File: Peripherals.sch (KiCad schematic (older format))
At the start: 62 parts, among them J10 Conn_01x01, J11 Conn_01x01, J12 Conn_01x01, J13 Conn_01x04, J14 RCAJack, J5 Conn_01x10, J6 Conn_01x10, J7 Conn_01x10, J8 Conn_01x08, J9 Conn_01x01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

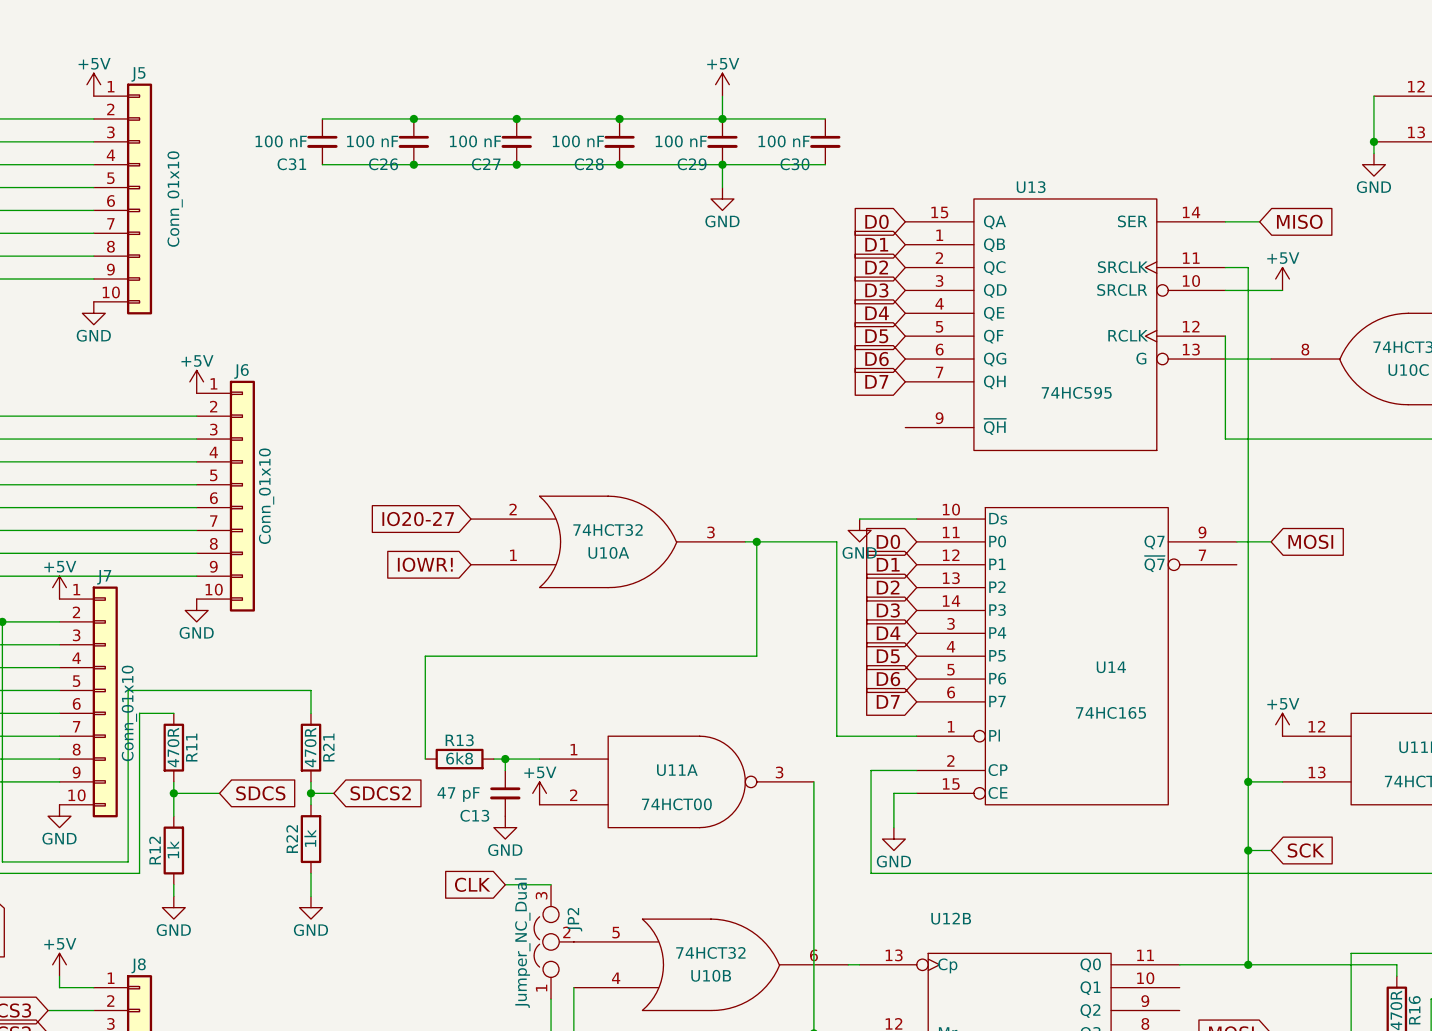
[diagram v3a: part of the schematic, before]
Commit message: Added SD card driver
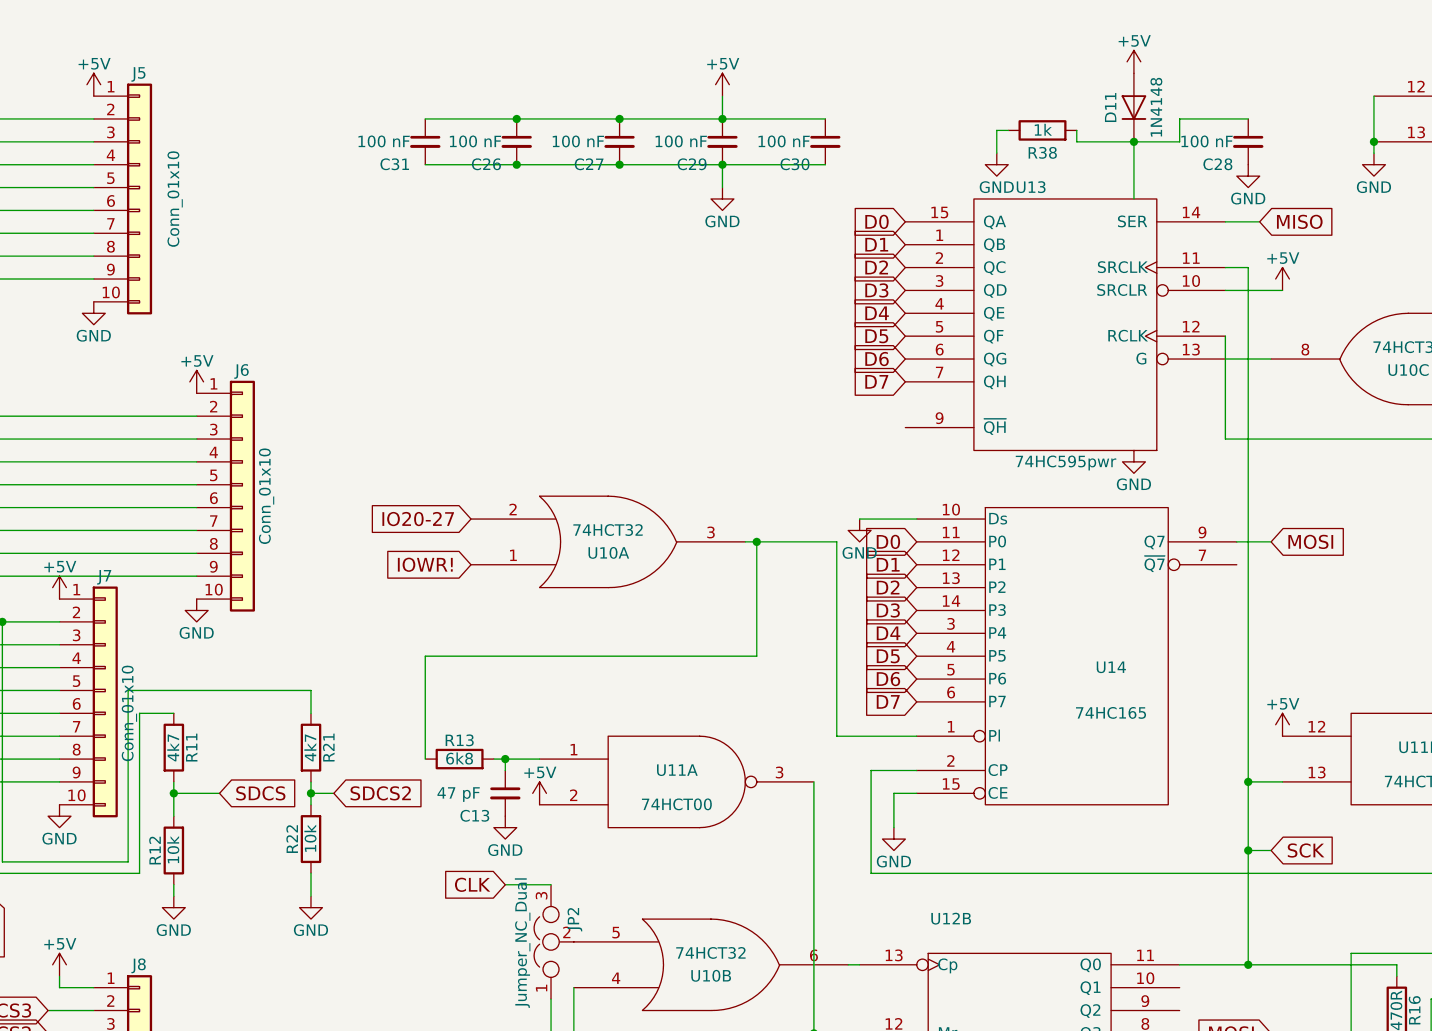
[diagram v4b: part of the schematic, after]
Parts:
- removed U13: 74HC595, Housings_DIP:DIP-16_W7.62mm_Socket, symbol 74HC595
- added D11: 1N4148, Diodes_THT:D_DO-35_SOD27_P7.62mm_Horizontal, symbol D
- added R38: 1k, Resistors_THT:R_Axial_DIN0207_L6.3mm_D2.5mm_P7.62mm_Horizontal, symbol R
- added U13: 74HC595pwr, symbol 74HC595pwr
- R11, R21: value 470R -> 4k7
- R12, R22: value 1k -> 10k
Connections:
- net +5V: now also D11.2 (A), U13.10 (SRCLR); no longer C28.1
- net D0: now also U13.15 (QA)
- net D1: now also U13.1 (QB)
- net D2: now also U13.2 (QC)
- net D3: now also U13.3 (QD)
- net D4: now also U13.4 (QE)
- net D5: now also U13.5 (QF)
- net D6: now also U13.6 (QG)
- net D7: now also U13.7 (QH)
- net GND: now also R38.1, U13.8 (GND)
- net MISO: now also U13.14 (SER)
- net SCK: now also U13.11 (SRCLK)
- net at U11.11, U14.2 (CP): now also U13.12 (RCLK)
- net at U10.8: now also U13.13 (G)
- new net: C28.1, D11.1 (K), R38.2, U13.16 (VCC)
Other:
- moved on the sheet: C26, C27, C28, C31
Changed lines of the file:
@@
 D7
 $Comp
-L +5V #PWR89
+L +5V #PWR92
 U 1 1 607EE7EE
 P 8950 1650
-F 0 "#PWR89" H 8950 1500 50  0001 C CNN
+F 0 "#PWR92" H 8950 1500 50  0001 C CNN
 F 1 "+5V" H 8950 1790 50  0000 C CNN
 F 2 "" H 8950 1650 50  0001 C CNN
@@
 	1    0    0    -1
 $EndComp
-$Comp
-L 74HC595 U13
-U 1 1 607EE4CE
-P 8000 1800
-F 0 "U13" H 8150 2400 50  0000 C CNN
-F 1 "74HC595" H 7950 1500 50  0000 C CNN
-F 2 "Housings_DIP:DIP-16_W7.62mm_Socket" H 8000 1800 50  0001 C CNN
-F 3 "" H 8000 1800 50  0001 C CNN
-	1    8000 1800
-	-1   0    0    -1
-$EndComp
 Text GLabel 8900 4900 0    60   Input ~ 0
 MOSI
@@
 $EndComp
 $Comp
-L GND #PWR91
+L GND #PWR94
 U 1 1 607928DE
 P 9050 5600
-F 0 "#PWR91" H 9050 5350 50  0001 C CNN
+F 0 "#PWR94" H 9050 5350 50  0001 C CNN
 F 1 "GND" H 9050 5450 50  0000 C CNN
 F 2 "" H 9050 5600 50  0001 C CNN
@@
 MISO
 $Comp
-L GND #PWR95
+L GND #PWR98
 U 1 1 60792D6A
 P 10050 6150
-F 0 "#PWR95" H 10050 5900 50  0001 C CNN
+F 0 "#PWR98" H 10050 5900 50  0001 C CNN
 F 1 "GND" H 10050 6000 50  0000 C CNN
 F 2 "" H 10050 6150 50  0001 C CNN
@@
 $EndComp
 $Comp
-L +5V #PWR97
+L +5V #PWR100
 U 1 1 60792FF2
 P 10350 2800
-F 0 "#PWR97" H 10350 2650 50  0001 C CNN
+F 0 "#PWR100" H 10350 2650 50  0001 C CNN
 F 1 "+5V" H 10350 2940 50  0000 C CNN
 F 2 "" H 10350 2800 50  0001 C CNN
@@
 $EndComp
 $Comp
-L GND #PWR94
+L GND #PWR97
 U 1 1 60793535
 P 9450 5350
-F 0 "#PWR94" H 9450 5100 50  0001 C CNN
+F 0 "#PWR97" H 9450 5100 50  0001 C CNN
 F 1 "GND" H 9450 5200 50  0000 C CNN
 F 2 "" H 9450 5350 50  0001 C CNN
@@
 $EndComp
 $Comp
-L GND #PWR98
+L GND #PWR101
 U 1 1 60794114
 P 10350 3850
-F 0 "#PWR98" H 10350 3600 50  0001 C CNN
+F 0 "#PWR101" H 10350 3600 50  0001 C CNN
 F 1 "GND" H 10350 3700 50  0000 C CNN
 F 2 "" H 10350 3850 50  0001 C CNN
@@
 $EndComp
 $Comp
-L GND #PWR99
+L GND #PWR102
 U 1 1 607945EF
 P 10900 3900
-F 0 "#PWR99" H 10900 3650 50  0001 C CNN
+F 0 "#PWR102" H 10900 3650 50  0001 C CNN
 F 1 "GND" H 10900 3750 50  0000 C CNN
 F 2 "" H 10900 3900 50  0001 C CNN
@@
 P 4100 3650
 F 0 "R11" V 4180 3650 50  0000 C CNN
-F 1 "470R" V 4100 3650 50  0000 C CNN
+F 1 "4k7" V 4100 3650 50  0000 C CNN
 F 2 "Resistors_THT:R_Axial_DIN0207_L6.3mm_D2.5mm_P7.62mm_Horizontal" V 4030 3650 50  0001 C CNN
 F 3 "" H 4100 3650 50  0001 C CNN
@@
 P 4100 4100
 F 0 "R12" V 4180 4100 50  0000 C CNN
-F 1 "1k" V 4100 4100 50  0000 C CNN
+F 1 "10k" V 4100 4100 50  0000 C CNN
 F 2 "Resistors_THT:R_Axial_DIN0207_L6.3mm_D2.5mm_P7.62mm_Horizontal" V 4030 4100 50  0001 C CNN
 F 3 "" H 4100 4100 50  0001 C CNN
@@
 $EndComp
 $Comp
-L +5V #PWR90
+L +5V #PWR93
 U 1 1 607AC0B6
 P 8950 3600
-F 0 "#PWR90" H 8950 3450 50  0001 C CNN
+F 0 "#PWR93" H 8950 3450 50  0001 C CNN
 F 1 "+5V" H 8950 3740 50  0000 C CNN
 F 2 "" H 8950 3600 50  0001 C CNN
@@
 P 4700 3650
 F 0 "R21" V 4780 3650 50  0000 C CNN
-F 1 "470R" V 4700 3650 50  0000 C CNN
+F 1 "4k7" V 4700 3650 50  0000 C CNN
 F 2 "Resistors_THT:R_Axial_DIN0207_L6.3mm_D2.5mm_P7.62mm_Horizontal" V 4630 3650 50  0001 C CNN
 F 3 "" H 4700 3650 50  0001 C CNN
@@
 P 4700 4050
 F 0 "R22" V 4780 4050 50  0000 C CNN
-F 1 "1k" V 4700 4050 50  0000 C CNN
+F 1 "10k" V 4700 4050 50  0000 C CNN
 F 2 "Resistors_THT:R_Axial_DIN0207_L6.3mm_D2.5mm_P7.62mm_Horizontal" V 4630 4050 50  0001 C CNN
 F 3 "" H 4700 4050 50  0001 C CNN
@@
 SDCS2
 $Comp
-L GND #PWR96
+L GND #PWR99
 U 1 1 607C336C
 P 10100 5150
-F 0 "#PWR96" H 10100 4900 50  0001 C CNN
+F 0 "#PWR99" H 10100 4900 50  0001 C CNN
 F 1 "GND" H 10100 5000 50  0000 C CNN
 F 2 "" H 10100 5150 50  0001 C CNN
@@
 MISO
 $Comp
-L +5V #PWR87
+L +5V #PWR89
 U 1 1 607C46A0
 P 8750 5300
-F 0 "#PWR87" H 8750 5150 50  0001 C CNN
+F 0 "#PWR89" H 8750 5150 50  0001 C CNN
 F 1 "+5V" H 8750 5440 50  0000 C CNN
 F 2 "" H 8750 5300 50  0001 C CNN
@@
 $EndComp
 $Comp
-L GND #PWR88
+L GND #PWR90
 U 1 1 607C50E0
 P 8750 6250
-F 0 "#PWR88" H 8750 6000 50  0001 C CNN
+F 0 "#PWR90" H 8750 6000 50  0001 C CNN
 F 1 "GND" H 8750 6100 50  0000 C CNN
 F 2 "" H 8750 6250 50  0001 C CNN
@@
 $EndComp
 $Comp
-L GND #PWR92
+L GND #PWR95
 U 1 1 607C528C
 P 9250 6300
-F 0 "#PWR92" H 9250 6050 50  0001 C CNN
+F 0 "#PWR95" H 9250 6050 50  0001 C CNN
 F 1 "GND" H 9250 6150 50  0000 C CNN
 F 2 "" H 9250 6300 50  0001 C CNN
@@
 L C_Small C28
 U 1 1 607C7786
-P 6050 1000
-F 0 "C28" H 5850 900 50  0000 L CNN
-F 1 "100 nF" H 5750 1000 50  0000 L CNN
-F 2 "Capacitors_THT:C_Disc_D5.0mm_W2.5mm_P2.50mm" H 6050 1000 50  0001 C CNN
-F 3 "" H 6050 1000 50  0001 C CNN
-	1    6050 1000
+P 8800 1000
+F 0 "C28" H 8600 900 50  0000 L CNN
+F 1 "100 nF" H 8500 1000 50  0000 L CNN
+F 2 "Capacitors_THT:C_Disc_D5.0mm_W2.5mm_P2.50mm" H 8800 1000 50  0001 C CNN
+F 3 "" H 8800 1000 50  0001 C CNN
+	1    8800 1000
 	1    0    0    -1
 $EndComp
@@
 L C_Small C27
 U 1 1 607C7A03
+P 6050 1000
+F 0 "C27" H 5850 900 50  0000 L CNN
+F 1 "100 nF" H 5750 1000 50  0000 L CNN
+F 2 "Capacitors_THT:C_Disc_D5.0mm_W2.5mm_P2.50mm" H 6050 1000 50  0001 C CNN
+F 3 "" H 6050 1000 50  0001 C CNN
+	1    6050 1000
+	1    0    0    -1
+$EndComp
+$Comp
+L C_Small C26
+U 1 1 607C7ABC
 P 5600 1000
-F 0 "C27" H 5400 900 50  0000 L CNN
+F 0 "C26" H 5400 900 50  0000 L CNN
 F 1 "100 nF" H 5300 1000 50  0000 L CNN
 F 2 "Capacitors_THT:C_Disc_D5.0mm_W2.5mm_P2.50mm" H 5600 1000 50  0001 C CNN
 F 3 "" H 5600 1000 50  0001 C CNN
 	1    5600 1000
-	1    0    0    -1
-$EndComp
-$Comp
-L C_Small C26
-U 1 1 607C7ABC
-P 5150 1000
-F 0 "C26" H 4950 900 50  0000 L CNN
-F 1 "100 nF" H 4850 1000 50  0000 L CNN
-F 2 "Capacitors_THT:C_Disc_D5.0mm_W2.5mm_P2.50mm" H 5150 1000 50  0001 C CNN
-F 3 "" H 5150 1000 50  0001 C CNN
-	1    5150 1000
 	1    0    0    -1
 $EndComp
@@
 L C_Small C31
 U 1 1 607ED9D2
-P 4750 1000
-F 0 "C31" H 4550 900 50  0000 L CNN
-F 1 "100 nF" H 4450 1000 50  0000 L CNN
-F 2 "Capacitors_THT:C_Disc_D5.0mm_W2.5mm_P2.50mm" H 4750 1000 50  0001 C CNN
-F 3 "" H 4750 1000 50  0001 C CNN
-	1    4750 1000
+P 5200 1000
+F 0 "C31" H 5000 900 50  0000 L CNN
+F 1 "100 nF" H 4900 1000 50  0000 L CNN
+F 2 "Capacitors_THT:C_Disc_D5.0mm_W2.5mm_P2.50mm" H 5200 1000 50  0001 C CNN
+F 3 "" H 5200 1000 50  0001 C CNN
+	1    5200 1000
 	1    0    0    -1
 $EndComp
@@
 $EndComp
 $Comp
-L GND #PWR93
+L GND #PWR96
 U 1 1 60888297
 P 9350 1050
-F 0 "#PWR93" H 9350 800 50  0001 C CNN
+F 0 "#PWR96" H 9350 800 50  0001 C CNN
 F 1 "GND" H 9350 900 50  0000 C CNN
 F 2 "" H 9350 1050 50  0001 C CNN
@@
 Wire Wire Line
 	2550 6300 2400 6300
-Connection ~ 5150 1100
-Connection ~ 5150 900
+Connection ~ 5600 1100
+Connection ~ 5600 900
 Wire Wire Line
 	3250 6300 3150 6300
@@
 Connection ~ 6500 900
 Connection ~ 6050 900
-Connection ~ 5600 900
-Wire Wire Line
-	4750 900  6950 900
-Connection ~ 5600 1100
 Connection ~ 6050 1100
 Connection ~ 6500 1100
 Wire Wire Line
-	4750 1100 6950 1100
+	5200 1100 6950 1100
 Wire Wire Line
 	3750 4800 3550 4800
@@
 Text GLabel 550  1400 3    60   Input ~ 0
 COLDRESET
+$Comp
+L +5V #PWR88
+U 1 1 6106EC6E
+P 8300 700
+F 0 "#PWR88" H 8300 550 50  0001 C CNN
+F 1 "+5V" H 8300 840 50  0000 C CNN
+F 2 "" H 8300 700 50  0001 C CNN
+F 3 "" H 8300 700 50  0001 C CNN
+	1    8300 700
+	1    0    0    -1
+$EndComp
+$Comp
+L D D11
+U 1 1 6106EEA1
+P 8300 850
+F 0 "D11" H 8300 950 50  0000 C CNN
+F 1 "1N4148" H 8300 750 50  0000 C CNN
+F 2 "Diodes_THT:D_DO-35_SOD27_P7.62mm_Horizontal" H 8300 850 50  0001 C CNN
+F 3 "" H 8300 850 50  0001 C CNN
+	1    8300 850
+	0    -1   -1   0
+$EndComp
+Wire Wire Line
+	8300 1000 8300 1250
+$Comp
+L GND #PWR87
+U 1 1 6106F360
+P 7700 1050
+F 0 "#PWR87" H 7700 800 50  0001 C CNN
+F 1 "GND" H 7700 900 50  0000 C CNN
+F 2 "" H 7700 1050 50  0001 C CNN
+F 3 "" H 7700 1050 50  0001 C CNN
+	1    7700 1050
+	1    0    0    -1
+$EndComp
+$Comp
+L R R38
+U 1 1 6106F862
+P 7900 950
+F 0 "R38" V 7800 950 50  0000 C CNN
+F 1 "1k" V 7900 950 50  0000 C CNN
+F 2 "Resistors_THT:R_Axial_DIN0207_L6.3mm_D2.5mm_P7.62mm_Horizontal" V 7830 950 50  0001 C CNN
+F 3 "" H 7900 950 50  0001 C CNN
+	1    7900 950
+	0    -1   -1   0
+$EndComp
+Wire Wire Line
+	8050 1000 8500 1000
+Wire Wire Line
+	8050 1000 8050 950
+Wire Wire Line
+	7700 1050 7700 950
+Wire Wire Line
+	7700 950  7750 950
+Wire Wire Line
+	8500 1000 8500 900
+Wire Wire Line
+	8500 900  8800 900
+Connection ~ 8300 1000
+$Comp
+L GND #PWR91
+U 1 1 610704B0
+P 8800 1100
+F 0 "#PWR91" H 8800 850 50  0001 C CNN
+F 1 "GND" H 8800 950 50  0000 C CNN
+F 2 "" H 8800 1100 50  0001 C CNN
+F 3 "" H 8800 1100 50  0001 C CNN
+	1    8800 1100
+	1    0    0    -1
+$EndComp
+Wire Wire Line
+	5200 900  6950 900
+$Comp
+L 74HC595pwr U13
+U 1 1 61070F3A
+P 8000 1800
+F 0 "U13" H 8150 2400 50  0000 C CNN
+F 1 "74HC595pwr" H 8000 1200 50  0000 C CNN
+F 2 "" H 8000 1800 50  0001 C CNN
+F 3 "" H 8000 1800 50  0001 C CNN
+	1    8000 1800
+	-1   0    0    -1
+$EndComp
+$Comp
+L GND #PWR?
+U 1 1 610712AE
+P 8300 2350
+F 0 "#PWR?" H 8300 2100 50  0001 C CNN
+F 1 "GND" H 8300 2200 50  0000 C CNN
+F 2 "" H 8300 2350 50  0001 C CNN
+F 3 "" H 8300 2350 50  0001 C CNN
+	1    8300 2350
+	1    0    0    -1
+$EndComp
 $EndSCHEMATC
